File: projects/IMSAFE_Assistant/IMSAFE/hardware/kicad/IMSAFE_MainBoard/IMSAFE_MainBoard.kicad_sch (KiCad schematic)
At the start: 0 parts

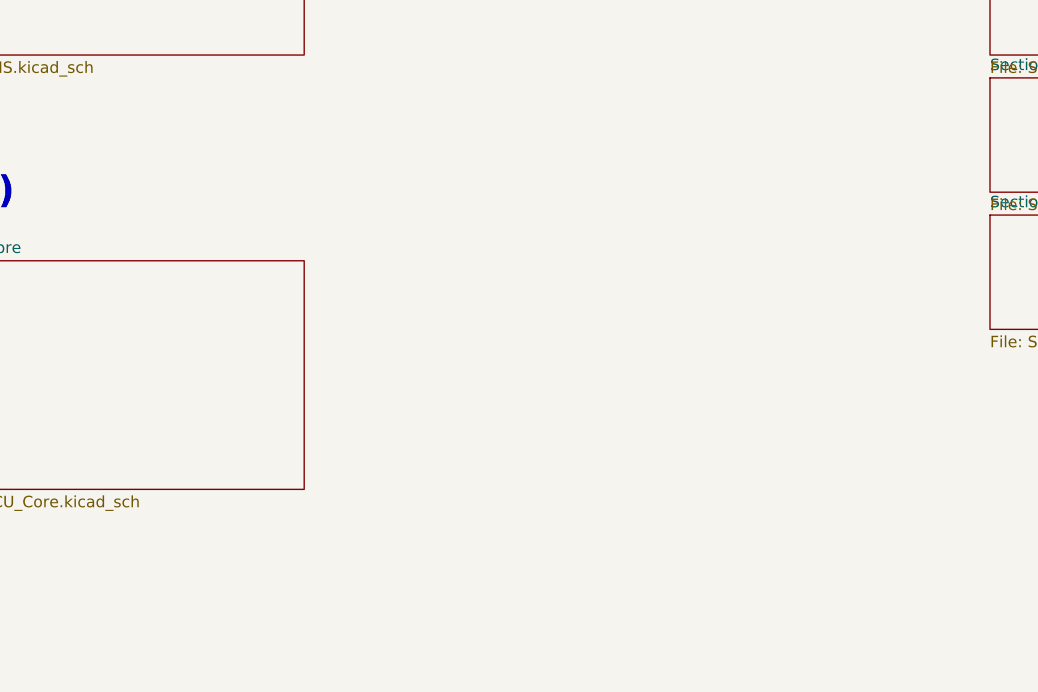
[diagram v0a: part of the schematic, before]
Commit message: Integrate Sections 14-16 into main hierarchical schematic
Add I/O Expander, Status LEDs, and Rotary Encoders sheets to the
root schematic with UI Sections label and page assignments 19-21.

Co-Authored-By: Claude Opus 4.5 <noreply@anthropic.com>
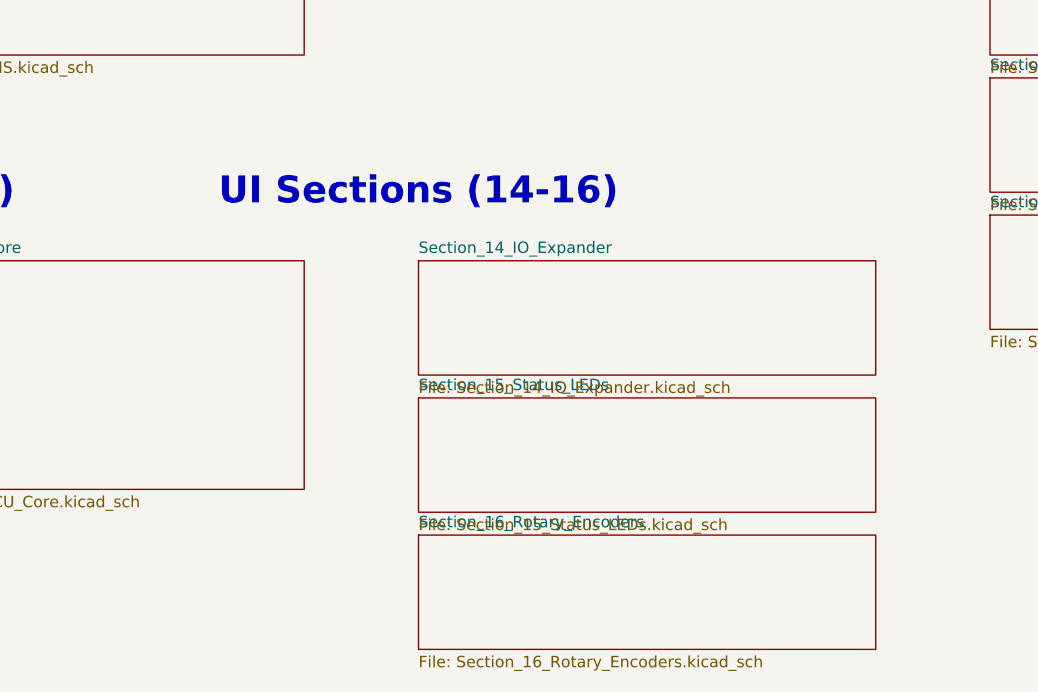
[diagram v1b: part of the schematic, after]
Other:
- added sheet Section_14_IO_Expander (Section_14_IO_Expander.kicad_sch)
- added sheet Section_15_Status_LEDs (Section_15_Status_LEDs.kicad_sch)
- added sheet Section_16_Rotary_Encoders (Section_16_Rotary_Encoders.kicad_sch)
- note added: "UI Sections (14-16)"
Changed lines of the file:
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@@
 		(uuid "mcu-label-001")
+	)
+	(text "UI Sections (14-16)"
+		(exclude_from_sim no)
+		(at 88.9 127 0)
+		(effects
+			(font
+				(size 3 3)
+				(bold yes)
+			)
+		)
+		(uuid "ui-label-001")
 	)
 	(text "Sensor Sections (7-11)"
@@
 				)
 			)
+		)
+	)
+	(sheet
+		(at 88.9 134.62)
+		(size 50.8 12.7)
+		(fields_autoplaced yes)
+		(stroke
+			(width 0.1524)
+			(type solid)
+		)
+		(fill
+			(color 255 224 194 1)
+		)
+		(uuid "sheet-sec14-ioexp")
+		(property "Sheetname" "Section_14_IO_Expander"
+			(at 88.9 133.9084 0)
+			(effects
+				(font
+					(size 1.27 1.27)
+				)
+				(justify left bottom)
+			)
+		)
+		(property "Sheetfile" "Section_14_IO_Expander.kicad_sch"
+			(at 88.9 147.9746 0)
+			(effects
+				(font
+					(size 1.27 1.27)
+				)
+				(justify left top)
+			)
+		)
+		(instances
+			(project "IMSAFE_MainBoard"
+				(path "/a1b2c3d4-e5f6-7890-abcd-ef1234567890"
+					(page "19")
+				)
+			)
+		)
+	)
+	(sheet
+		(at 88.9 149.86)
+		(size 50.8 12.7)
+		(fields_autoplaced yes)
+		(stroke
+			(width 0.1524)
+			(type solid)
+		)
+		(fill
+			(color 255 224 194 1)
+		)
+		(uuid "sheet-sec15-leds")
+		(property "Sheetname" "Section_15_Status_LEDs"
+			(at 88.9 149.1484 0)
+			(effects
+				(font
+					(size 1.27 1.27)
+				)
+				(justify left bottom)
+			)
+		)
+		(property "Sheetfile" "Section_15_Status_LEDs.kicad_sch"
+			(at 88.9 163.2146 0)
+			(effects
+				(font
+					(size 1.27 1.27)
+				)
+				(justify left top)
+			)
+		)
+		(instances
+			(project "IMSAFE_MainBoard"
+				(path "/a1b2c3d4-e5f6-7890-abcd-ef1234567890"
+					(page "20")
+				)
+			)
+		)
+	)
+	(sheet
+		(at 88.9 165.1)
+		(size 50.8 12.7)
+		(fields_autoplaced yes)
+		(stroke
+			(width 0.1524)
+			(type solid)
+		)
+		(fill
+			(color 255 224 194 1)
+		)
+		(uuid "sheet-sec16-enc")
+		(property "Sheetname" "Section_16_Rotary_Encoders"
+			(at 88.9 164.3884 0)
+			(effects
+				(font
+					(size 1.27 1.27)
+				)
+				(justify left bottom)
+			)
+		)
+		(property "Sheetfile" "Section_16_Rotary_Encoders.kicad_sch"
+			(at 88.9 178.4546 0)
+			(effects
+				(font
+					(size 1.27 1.27)
+				)
+				(justify left top)
+			)
+		)
+		(instances
+			(project "IMSAFE_MainBoard"
+				(path "/a1b2c3d4-e5f6-7890-abcd-ef1234567890"
+					(page "21")
+				)
+			)

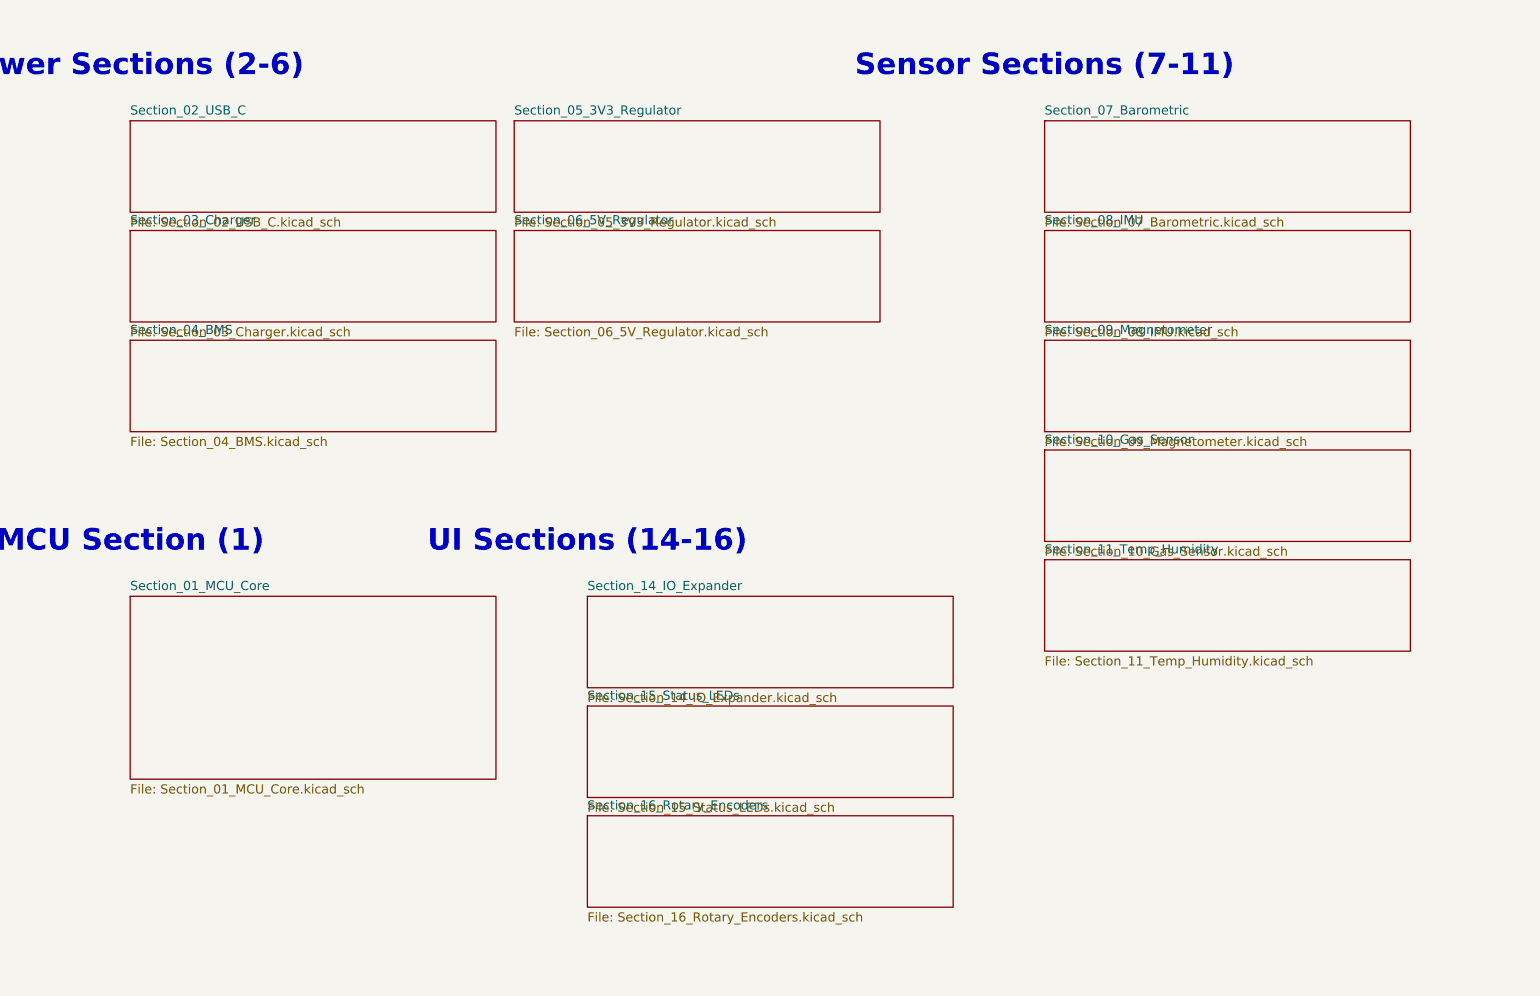
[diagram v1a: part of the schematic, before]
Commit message: Add hierarchical sheet pins to root schematic
Add sheet pins to connect child sheet hierarchical labels:
- Section 02: USB_DP, USB_DM, VBUS
- Section 03: VBUS, VSYS, VBAT, CHG_INT, I2C4_SDA, I2C4_SCL
- Section 04: VBAT, VSYS, CELL_MID, PACK_NEG
- Section 05: VSYS, +3V3
- Section 06: VSYS, +5V
- Section 01: HSE_IN/OUT, LSE_IN/OUT, NRST, BOOT0
- Section 07: I2C1_SDA, I2C1_SCL, BARO_INT
- Section 14: I2C1_SDA, I2C1_SCL, INTA, INTB
- Section 15: LED_DATA
- Section 16: ENC1_A/B/SW, ENC2_A/B/SW

Reduces ERC hier_label_mismatch from 36 to 1.

Co-Authored-By: Claude Opus 4.5 <noreply@anthropic.com>
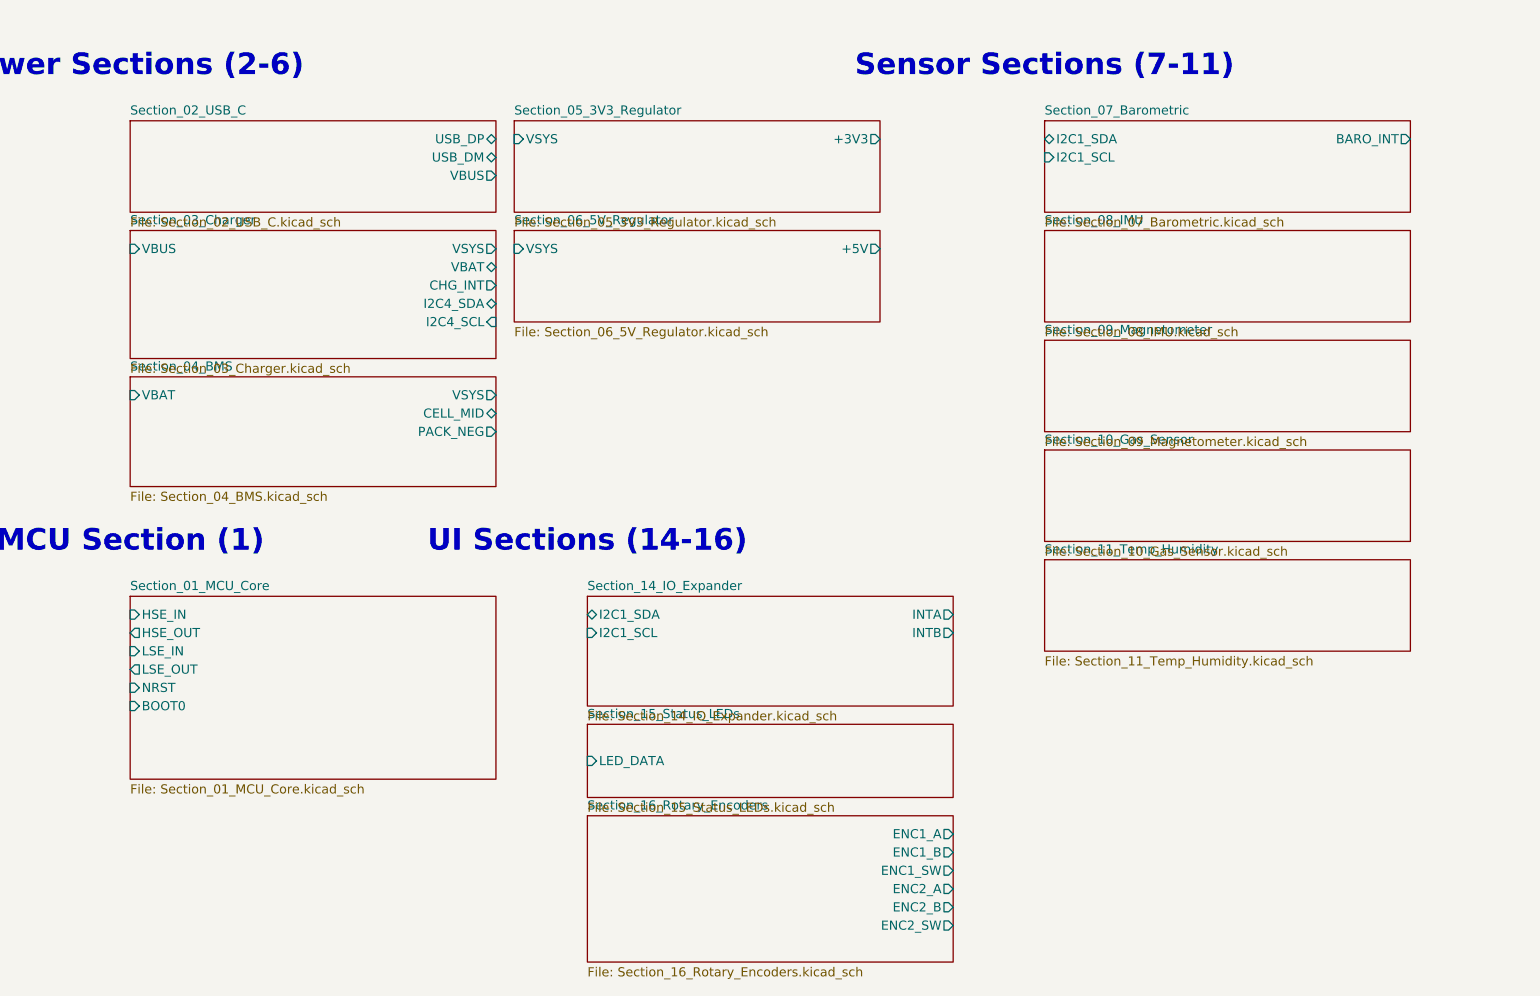
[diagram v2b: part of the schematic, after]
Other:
- sheet Section_01_MCU_Core ports: added BOOT0, HSE_IN, HSE_OUT, LSE_IN, LSE_OUT, NRST; removed none
- sheet Section_02_USB_C ports: added USB_DM, USB_DP, VBUS; removed none
- sheet Section_03_Charger ports: added CHG_INT, I2C4_SCL, I2C4_SDA, VBAT, VBUS, VSYS; removed none
- sheet Section_04_BMS ports: added CELL_MID, PACK_NEG, VBAT, VSYS; removed none
- sheet Section_05_3V3_Regulator ports: added +3V3, VSYS; removed none
- sheet Section_06_5V_Regulator ports: added +5V, VSYS; removed none
- sheet Section_07_Barometric ports: added BARO_INT, I2C1_SCL, I2C1_SDA; removed none
- sheet Section_14_IO_Expander ports: added I2C1_SCL, I2C1_SDA, INTA, INTB; removed none
- sheet Section_15_Status_LEDs ports: added LED_DATA; removed none
- sheet Section_16_Rotary_Encoders ports: added ENC1_A, ENC1_B, ENC1_SW, ENC2_A, ENC2_B, ENC2_SW; removed none
